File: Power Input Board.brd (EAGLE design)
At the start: 136.7 x 125.3 mm, 16 parts, among them Q1 SPB80P06P

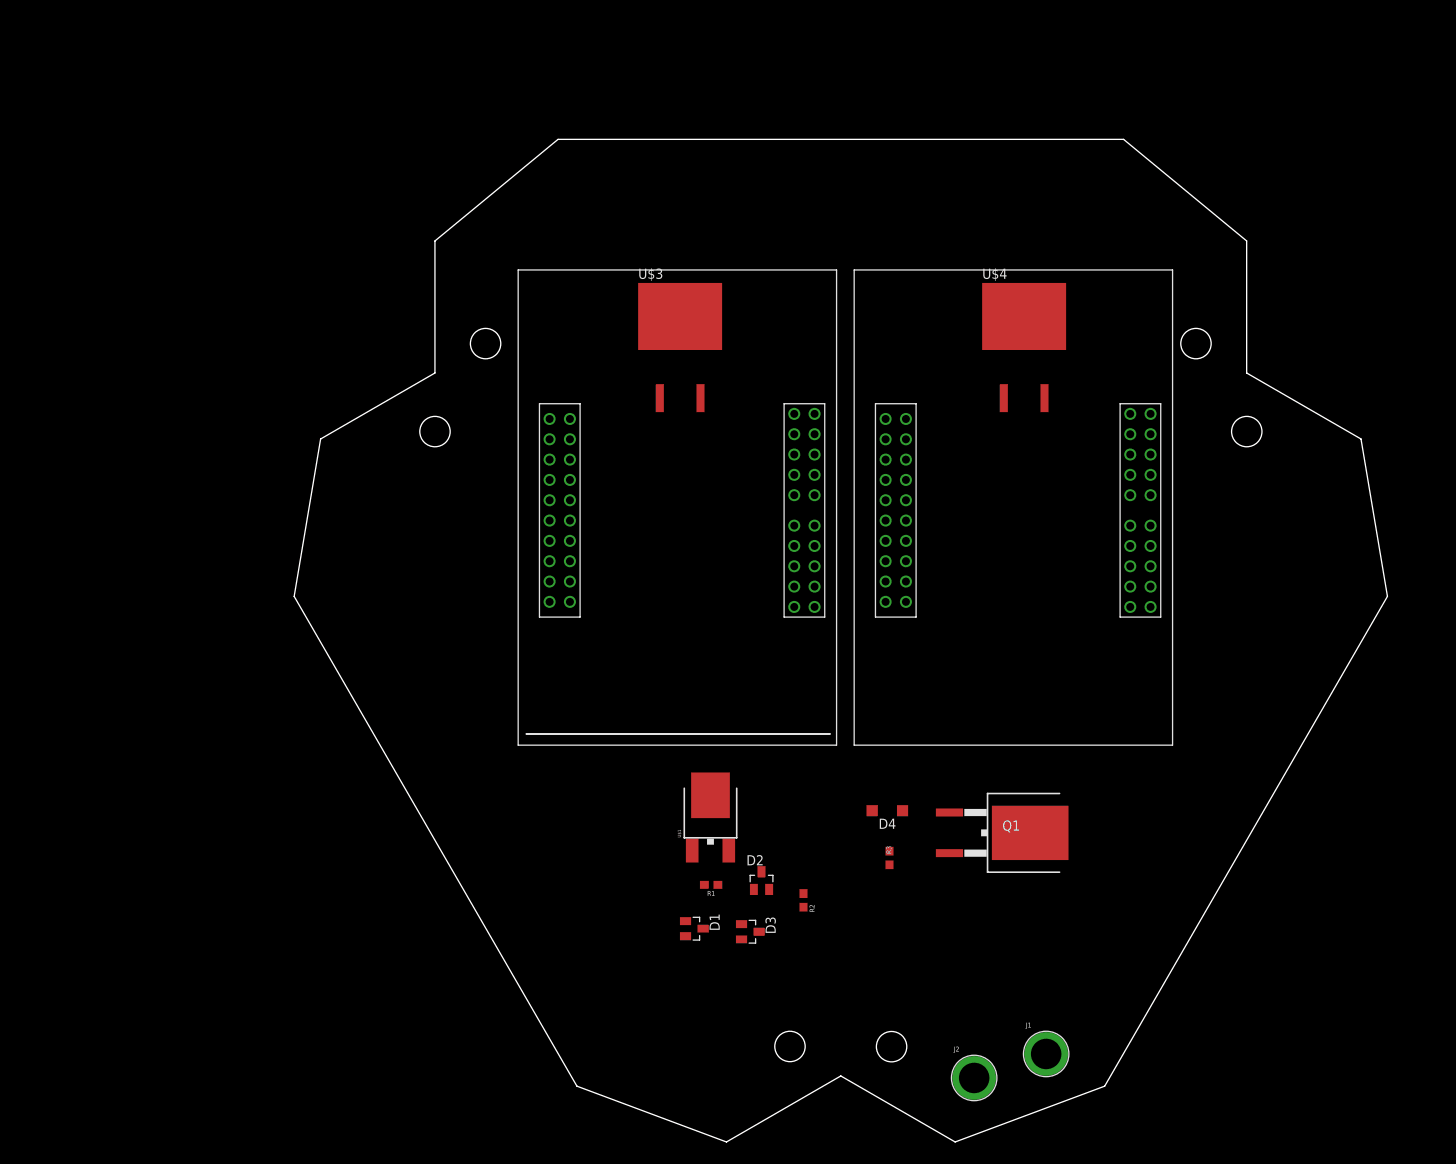
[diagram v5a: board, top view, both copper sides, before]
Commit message: added connectors
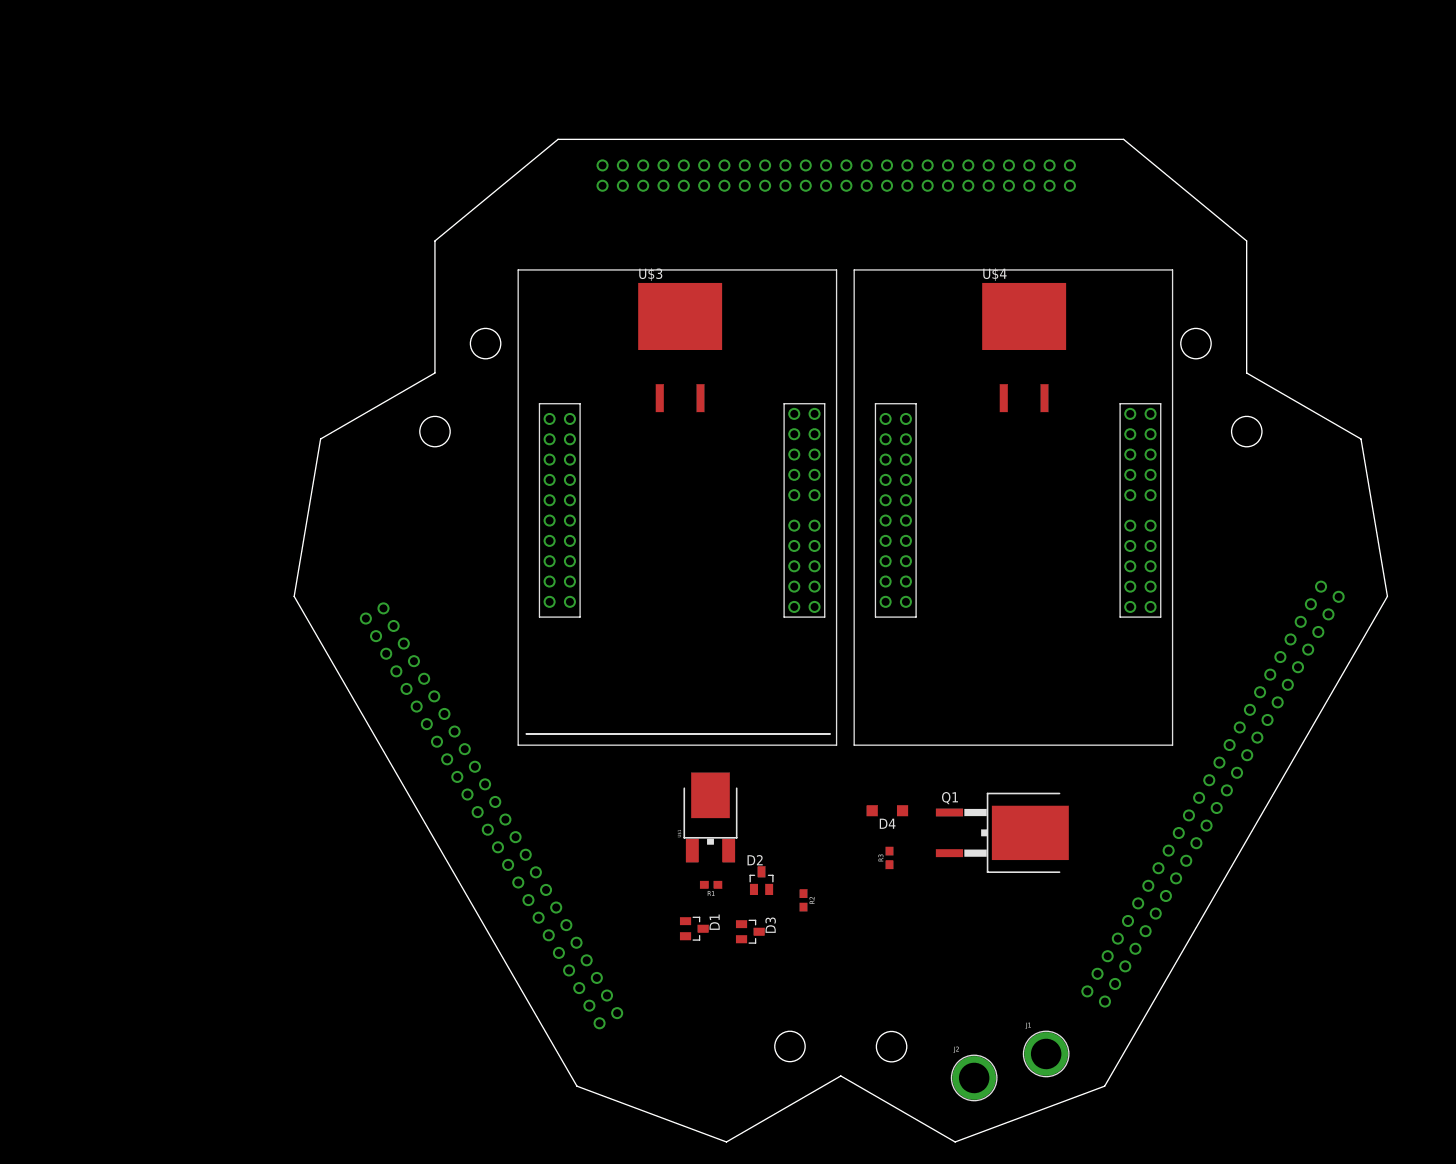
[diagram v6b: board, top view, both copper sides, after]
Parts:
- added U$7, U$8, U$9: PDB_PCB_CONNEC, PDB_PCB_connectors:PDB_PCB
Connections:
- net +12V: now also U$7.+12V1, U$7.+12V10, U$7.+12V11, U$7.+12V12, U$7.+12V13, U$7.+12V14, U$7.+12V15, U$7.+12V16, U$7.+12V17, U$7.+12V18, U$7.+12V19, U$7.+12V2, U$7.+12V20, U$7.+12V21, U$7.+12V22, U$7.+12V23, U$7.+12V24, U$7.+12V3, U$7.+12V4, U$7.+12V5, U$7.+12V6, U$7.+12V7, U$7.+12V8, U$7.+12V9, U$8.+12V1, U$8.+12V10, U$8.+12V11, U$8.+12V12, U$8.+12V13, U$8.+12V14, U$8.+12V15, U$8.+12V16, U$8.+12V17, U$8.+12V18, U$8.+12V19, U$8.+12V2, U$8.+12V20, U$8.+12V21, U$8.+12V22, U$8.+12V23, U$8.+12V24, U$8.+12V3, U$8.+12V4, U$8.+12V5, U$8.+12V6, U$8.+12V7, U$8.+12V8, U$8.+12V9, U$9.+12V1, U$9.+12V10, U$9.+12V11, U$9.+12V12, U$9.+12V13, U$9.+12V14, U$9.+12V15, U$9.+12V16, U$9.+12V17, U$9.+12V18, U$9.+12V19, U$9.+12V2, U$9.+12V20, U$9.+12V21, U$9.+12V22, U$9.+12V23, U$9.+12V24, U$9.+12V3, U$9.+12V4, U$9.+12V5, U$9.+12V6, U$9.+12V7, U$9.+12V8, U$9.+12V9
- net GND: now also U$7.GND10, U$7.GND11, U$7.GND12, U$7.GND13, U$7.GND14, U$7.GND15, U$7.GND16, U$7.GND17, U$7.GND18, U$7.GND19, U$7.GND2, U$7.GND20, U$7.GND21, U$7.GND22, U$7.GND23, U$7.GND24, U$7.GND3, U$7.GND4, U$7.GND5, U$7.GND6, U$7.GND7, U$7.GND8, U$7.GND9, U$8.GND10, U$8.GND11, U$8.GND12, U$8.GND13, U$8.GND14, U$8.GND15, U$8.GND16, U$8.GND17, U$8.GND18, U$8.GND19, U$8.GND2, U$8.GND20, U$8.GND21, U$8.GND22, U$8.GND23, U$8.GND24, U$8.GND3, U$8.GND4, U$8.GND5, U$8.GND6, U$8.GND7, U$8.GND8, U$8.GND9, U$9.GND10, U$9.GND11, U$9.GND12, U$9.GND13, U$9.GND14, U$9.GND15, U$9.GND16, U$9.GND17, U$9.GND18, U$9.GND19, U$9.GND2, U$9.GND20, U$9.GND21, U$9.GND22, U$9.GND23, U$9.GND24, U$9.GND3, U$9.GND4, U$9.GND5, U$9.GND6, U$9.GND7, U$9.GND8, U$9.GND9

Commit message: routed roughly
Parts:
- moved D4 13.2 mm to (85.8, 47.5)
- moved R3 9.61 mm to (77.7, 44.5), flipped to the bottom, turned to 180 degrees
- moved D2 8.86 mm to (53.3, 39.9)
- moved U$1 7.54 mm to (44.9, 44.1)
- moved R1 7.28 mm to (44.9, 32.9)
- moved R2 6.36 mm to (58.3, 33.6)
- moved Q1 5.01 mm to (83.7, 37.2), turned to 90 degrees
- moved D1 4.81 mm to (45.2, 27.0)
- moved D3 4.05 mm to (53.0, 26.1)
- moved J2 3.70 mm to (82.3, 10.5)
- moved J1 2.63 mm to (91.4, 10.7)
- moved U$6 1.27 mm to (68.7, 109.0)
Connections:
- removed net +48V_GND: U$6.48V_GND1, U$6.48V_GND2, U$6.48V_GND3, U$6.48V_GND4
- net 48V_GND: now also U$6.48V_GND1, U$6.48V_GND2, U$6.48V_GND3, U$6.48V_GND4
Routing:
- net +12V: track 0.00 -> 250.4 mm
- net ON/OFF: track 0.00 -> 135.6 mm, vias 0 -> 2
- net N$3: track 0.00 -> 14.9 mm, vias 0 -> 1
- net 3.3V: track 0.00 -> 11.7 mm
- net N$2: track 0.00 -> 11.5 mm
- net N$5: track 0.00 -> 8.38 mm
- net N$1: track 0.00 -> 5.58 mm
- added copper zone on layer 1, net +12V
- added copper zone on layer 1, net +12V_1
- added copper zone on layer 1, net +12V_2
- added copper zone on layer 1, net +48V
- added copper zone on layer 1, net +48V_RAW
- added copper zone on layer 16, net 48V_GND
- added copper zone on layer 16, net GND

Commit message: fixed airwire
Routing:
- net ON/OFF: track 135.6 -> 129.0 mm
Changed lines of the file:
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@@
 <?xml version="1.0" encoding="utf-8"?>
 <!DOCTYPE eagle SYSTEM "eagle.dtd">
-<eagle version="9.2.0">
+<eagle version="9.1.3">
 <drawing>
 <settings>
@@
 <wire x1="29.2862" y1="86.233" x2="30.8882" y2="87.835" width="0.8128" layer="16"/>
 <wire x1="30.8882" y1="87.835" x2="31.93" y2="87.835" width="0.8128" layer="16"/>
-<wire x1="50.4896" y1="45.7002" x2="52.1604" y2="47.371" width="0.8128" layer="1"/>
-<wire x1="52.1604" y1="47.371" x2="52.2478" y2="47.371" width="0.8128" layer="1"/>
-<via x="52.2478" y="47.371" extent="1-16" drill="0.35"/>
-<wire x1="52.2478" y1="47.371" x2="65.5574" y2="47.371" width="0.8128" layer="16"/>
-<wire x1="65.5574" y1="47.371" x2="69.8246" y2="51.6382" width="0.8128" layer="16"/>
-<wire x1="69.8246" y1="51.6382" x2="69.8246" y2="85.8774" width="0.8128" layer="16"/>
 <wire x1="71.8076" y1="87.8604" x2="72.66" y2="87.8604" width="0.8128" layer="16"/>
-<wire x1="69.8246" y1="85.8774" x2="71.8076" y2="87.8604" width="0.8128" layer="16"/>
+<wire x1="71.8076" y1="87.8604" x2="69.8246" y2="85.8774" width="0.8128" layer="16"/>
+<wire x1="69.8246" y1="85.8774" x2="69.7992" y2="62.8142" width="0.8128" layer="16"/>
+<via x="69.7992" y="62.8142" extent="1-16" drill="0.35"/>
+<wire x1="69.7992" y1="62.8142" x2="54.356" y2="47.371" width="0.8128" layer="1"/>
+<wire x1="52.1604" y1="47.371" x2="50.4896" y2="45.7002" width="0.8128" layer="1"/>
+<wire x1="54.356" y1="47.371" x2="52.1604" y2="47.371" width="0.8128" layer="1"/>
 </signal>
 <signal name="N$5">
@@
 <vertex x="86.5886" y="37.8968"/>
 <vertex x="94.5642" y="37.8968"/>
-<vertex x="94.5642" y="74.9046"/>
-<vertex x="79.1718" y="74.9046"/>
+<vertex x="94.5642" y="73.66"/>
+<vertex x="79.1718" y="73.66"/>
 <vertex x="79.1718" y="84.1248"/>
 <vertex x="70.6628" y="84.1248"/>
@@
 <vertex x="70.8406" y="7.2898"/>
 </polygon>
-<wire x1="34.47" y1="70.055" x2="72.66" y2="70.0804" width="0" layer="19" extent="1-1"/>
 </signal>
 <signal name="+48V_RAW">
